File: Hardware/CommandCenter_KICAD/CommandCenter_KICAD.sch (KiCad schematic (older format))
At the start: 49 parts

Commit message: Layout started
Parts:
- removed D?: LED, LEDs:LED_0603_HandSoldering, symbol Device:LED
- removed J?: BAT+, NFC_Toy_Lib:Pad_SMD_Small, symbol Pad:Pad
- removed J?: BAT-, NFC_Toy_Lib:Pad_SMD_Small, symbol Pad:Pad
- removed J?: MOT_SW0, NFC_Toy_Lib:Pad_SMD_Small, symbol Pad:Pad
- removed J?: MOT_SW1, NFC_Toy_Lib:Pad_SMD_Small, symbol Pad:Pad
- removed J?: MOT_SW2, NFC_Toy_Lib:Pad_SMD_Small, symbol Pad:Pad
- removed J?: MOT_SW_RTN, NFC_Toy_Lib:Pad_SMD_Small, symbol Pad:Pad
- removed R?: 121, Resistors_SMD:R_0603_HandSoldering, symbol Device:R
- removed R?: 10k, Resistors_SMD:R_0603_HandSoldering, symbol Device:R
- added J1: Battery, Connector_JST:JST_PH_S2B-PH-K_1x02_P2.00mm_Horizontal, symbol Connector_Generic:Conn_01x02
- added J2: Motor_Switches, Connector_PinHeader_2.54mm:PinHeader_1x04_P2.54mm_Vertical, symbol Connector_Generic:Conn_01x04
- added Q1, Q2: DMG1012T-7, digikey-footprints:SOT-523, symbol dk_Transistors-FETs-MOSFETs-Single:DMG1012T-7
- added R1, R2, R8: 10k, Resistor_SMD:R_0603_1608Metric_Pad1.05x0.95mm_HandSolder, symbol Device:R
- added R13: 100k, Resistor_SMD:R_0603_1608Metric_Pad1.05x0.95mm_HandSolder, symbol Device:R
- C1, C2, C3, C4, C5: renamed from C?; footprint Capacitors_SMD:C_0402 -> Capacitor_SMD:C_0603_1608Metric_Pad1.05x0.95mm_HandSolder
- C10: renamed from C?; footprint Capacitors_SMD:C_1206_HandSoldering -> Capacitor_SMD:C_1206_3216Metric_Pad1.42x1.75mm_HandSolder
- C11, C12, C7, C8, C9: renamed from C?; footprint Capacitors_SMD:C_0603_HandSoldering -> Capacitor_SMD:C_0603_1608Metric_Pad1.05x0.95mm_HandSolder
- C6: renamed from C?; footprint Capacitors_SMD:C_0402 -> Capacitor_SMD:C_0402_1005Metric
- D1: renamed from D?; footprint LEDs:LED_0603_HandSoldering -> LED_SMD:LED_0603_1608Metric_Pad1.05x0.95mm_HandSolder
- J3: renamed from J?; footprint Socket_Strips:Socket_Strip_Straight_2x05_Pitch2.54mm_SMD -> CommandCenter:JLink_Mini_0p05
- J4: renamed from J?; footprint (none) -> Connector_PinHeader_2.54mm:PinHeader_1x03_P2.54mm_Vertical
- L1: renamed from L?; footprint Inductors_SMD:L_12x12mm_h4.5mm -> Inductor_SMD:L_12x12mm_H4.5mm
- MK1, MK2, MK3, MK4: renamed from MK?; footprint Mounting_Holes:MountingHole_2.5mm -> MountingHole:MountingHole_3.2mm_M3
- R10, R11, R12, R14, R3, R4, R5, R6, R7, R9: renamed from R?; footprint Resistors_SMD:R_0603_HandSoldering -> Resistor_SMD:R_0603_1608Metric_Pad1.05x0.95mm_HandSolder
- TP1, TP2, TP3, TP4, TP5, TP6, TP7: renamed from TP?; footprint (none) -> TestPoint:TestPoint_Pad_2.0x2.0mm
- U1: renamed from U?; footprint NFC_Toy_Lib:SOP65P640X120-17N -> CommandCenter:SOP65P640X120-17N
- U2: renamed from U?; footprint NFC_Toy_Lib:QFP50P900X900X160-48N -> CommandCenter:QFP50P900X900X160-48N
- U3: renamed from U?; footprint TO_SOT_Packages_SMD:SOT-23-5 -> Package_TO_SOT_SMD:SOT-23-5
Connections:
- net +3V3: now also R13.1
- net +BATT: now also J1.1 (Pin_1), R2.1, R8.1
- net GND: now also J1.2 (Pin_2), J2.4 (Pin_4), Q1.2 (S), Q2.2 (S), R1.2
- net SWDIO_AUDIO: now also R13.2
- net at R10.2, U2.18 (PB0): now also J2.1 (Pin_1)
- net at R11.2, U2.19 (PB1): now also J2.2 (Pin_2)
- net at R12.2, U2.20 (PB2): now also J2.3 (Pin_3)
- net AUDIO_UART_TX: now reaches U2.30 (PA9)
- net AUDIO_UART_RX: now reaches U2.31 (PA10)
- net AUDIO_SD_N_1: now reaches U2.4 (PC15OSC32_OUT)
- net 5V_ENB renamed PWR_ENB_3V
- net PWR_ENB_3V: now also Q1.1 (G), R1.1; no longer U1.9 (EN)
- net AUDIO_SD_N renamed AUDIO_SD_N_0
- new net: Q1.3 (D), Q2.1 (G), R2.2
- new net PWR_ENB_5V: Q2.3 (D), R8.2, U1.9 (EN)
- no-connect marks 11 -> 21
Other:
- moved on the sheet: C10, C11, C12, C6, C7, C8, C9, J3, J4, L1, MK1, MK2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

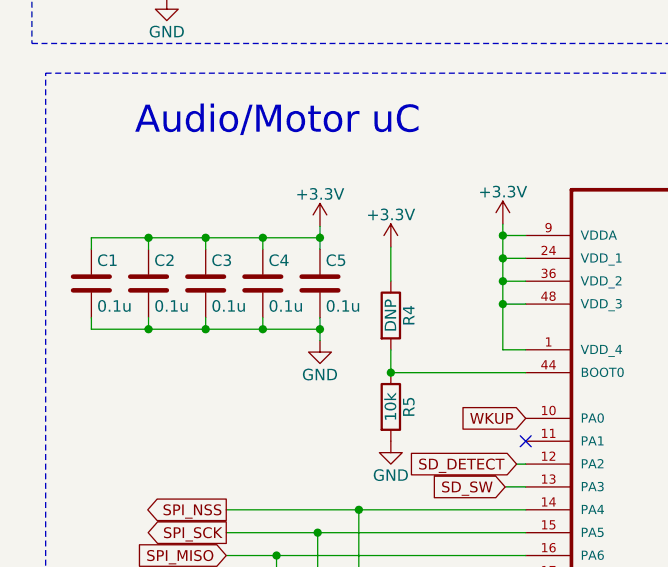
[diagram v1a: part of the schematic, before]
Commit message: Light Project Stable
DotStars and bar graph working. Getting master read nack on I2C to color sensor.
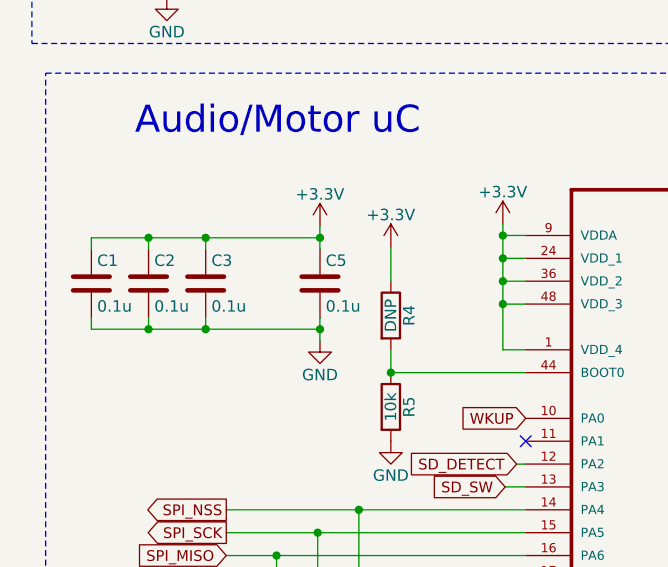
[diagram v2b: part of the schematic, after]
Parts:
- removed C4: 0.1u, Capacitor_SMD:C_0603_1608Metric_Pad1.05x0.95mm_HandSolder, symbol Device:C
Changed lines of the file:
@@
-$EndComp
-$Comp
-L Device:C C4
-U 1 1 5ACF4FF3
-P 1560 4460
-F 0 "C4" H 1585 4560 50  0000 L CNN
-F 1 "0.1u" H 1585 4360 50  0000 L CNN
-F 2 "Capacitor_SMD:C_0603_1608Metric_Pad1.05x0.95mm_HandSolder" H 1598 4310 50  0001 C CNN
-F 3 "" H 1560 4460 50  0001 C CNN
-	1    1560 4460
-	1    0    0    -1
 $EndComp
 $Comp
@@
 Wire Wire Line
 	1060 4660 1310 4660
-Wire Wire Line
-	1310 4660 1560 4660
-Wire Wire Line
-	1560 4660 1810 4660
 Connection ~ 1810 4660
 Wire Wire Line
@@
 Wire Wire Line
 	1060 4260 1310 4260
-Wire Wire Line
-	1310 4260 1560 4260
-Wire Wire Line
-	1560 4260 1810 4260
 Connection ~ 1810 4260
-Wire Wire Line
-	1560 4310 1560 4260
-Connection ~ 1560 4260
 Wire Wire Line
 	1310 4310 1310 4260
@@
 	1310 4610 1310 4660
 Connection ~ 1310 4660
-Wire Wire Line
-	1560 4610 1560 4660
-Connection ~ 1560 4660
 Wire Wire Line
 	2710 6250 1710 6250
@@
 Wire Wire Line
 	1480 2950 1480 3000
+Wire Wire Line
+	1310 4260 1810 4260
+Wire Wire Line
+	1310 4660 1810 4660
 $EndSCHEMATC
